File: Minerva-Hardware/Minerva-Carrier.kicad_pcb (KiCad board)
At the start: 4 copper layers, 83.5 x 90 mm, 58 parts, among them J11 USB_C_Receptacle_USB2.0, J14 JST_SHBM04B-SRSS-TB, J16 Conn_01x22_Female, J2 Conn_02x07_Odd_Even, J4 Bus_M.2_Socket_M, J5 Conn_01x22_Female, J6 THD-02-R, J8 THD-20-R, Q2 RQ6E080AJ, SW1 Right angle Tact button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

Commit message: renames
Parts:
- moved J2 76.2 mm to (153.0, 134.7), turned to 0 degrees
- moved J8 65.4 mm to (84.0, 85.2), turned to 0 degrees
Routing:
- net /+5v: track 272.6 -> 274.1 mm
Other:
- board text removed: "J3 : nBT_Dis GND"
- board text removed: "Raspberry Pi HAT"
- board text removed: "nWireless_Dis"

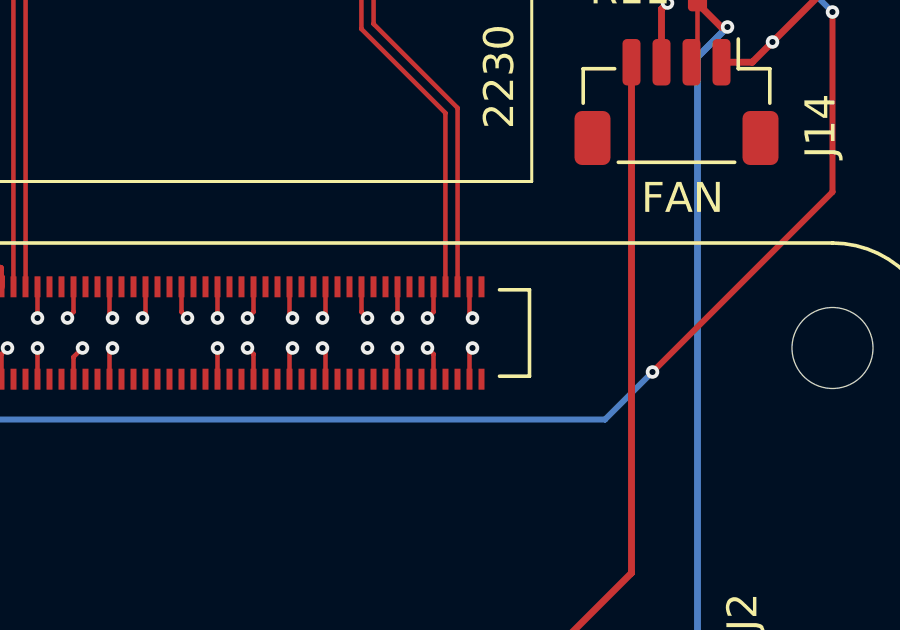
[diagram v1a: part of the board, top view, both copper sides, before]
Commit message: Update KiCad and start working on the faceplate pcb
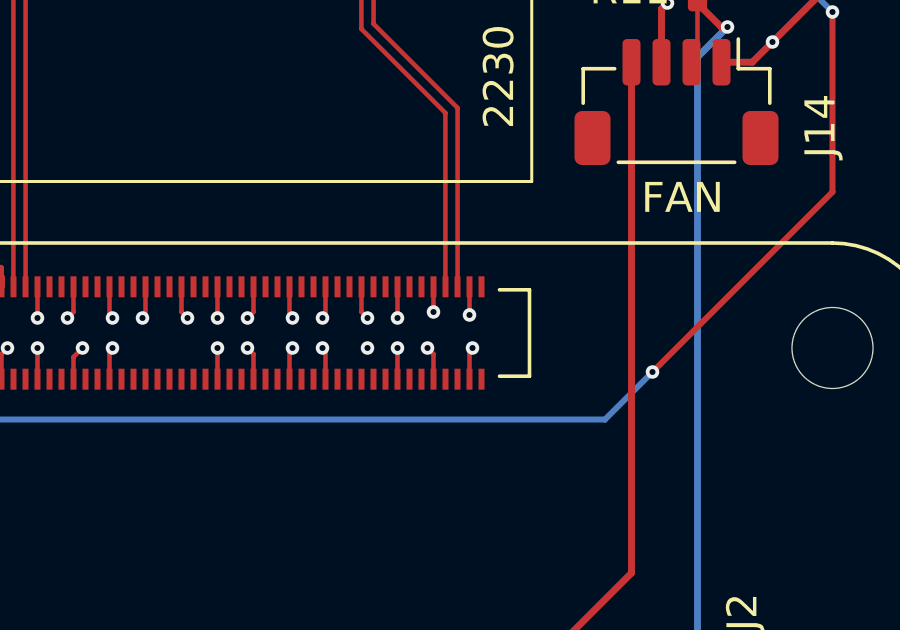
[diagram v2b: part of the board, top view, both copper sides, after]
